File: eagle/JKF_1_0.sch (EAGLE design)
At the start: 14 parts, among them IC1 74HC107N, X1 In A, X2 In B, X3 Ctrl, X4 Out A, X5 Out B

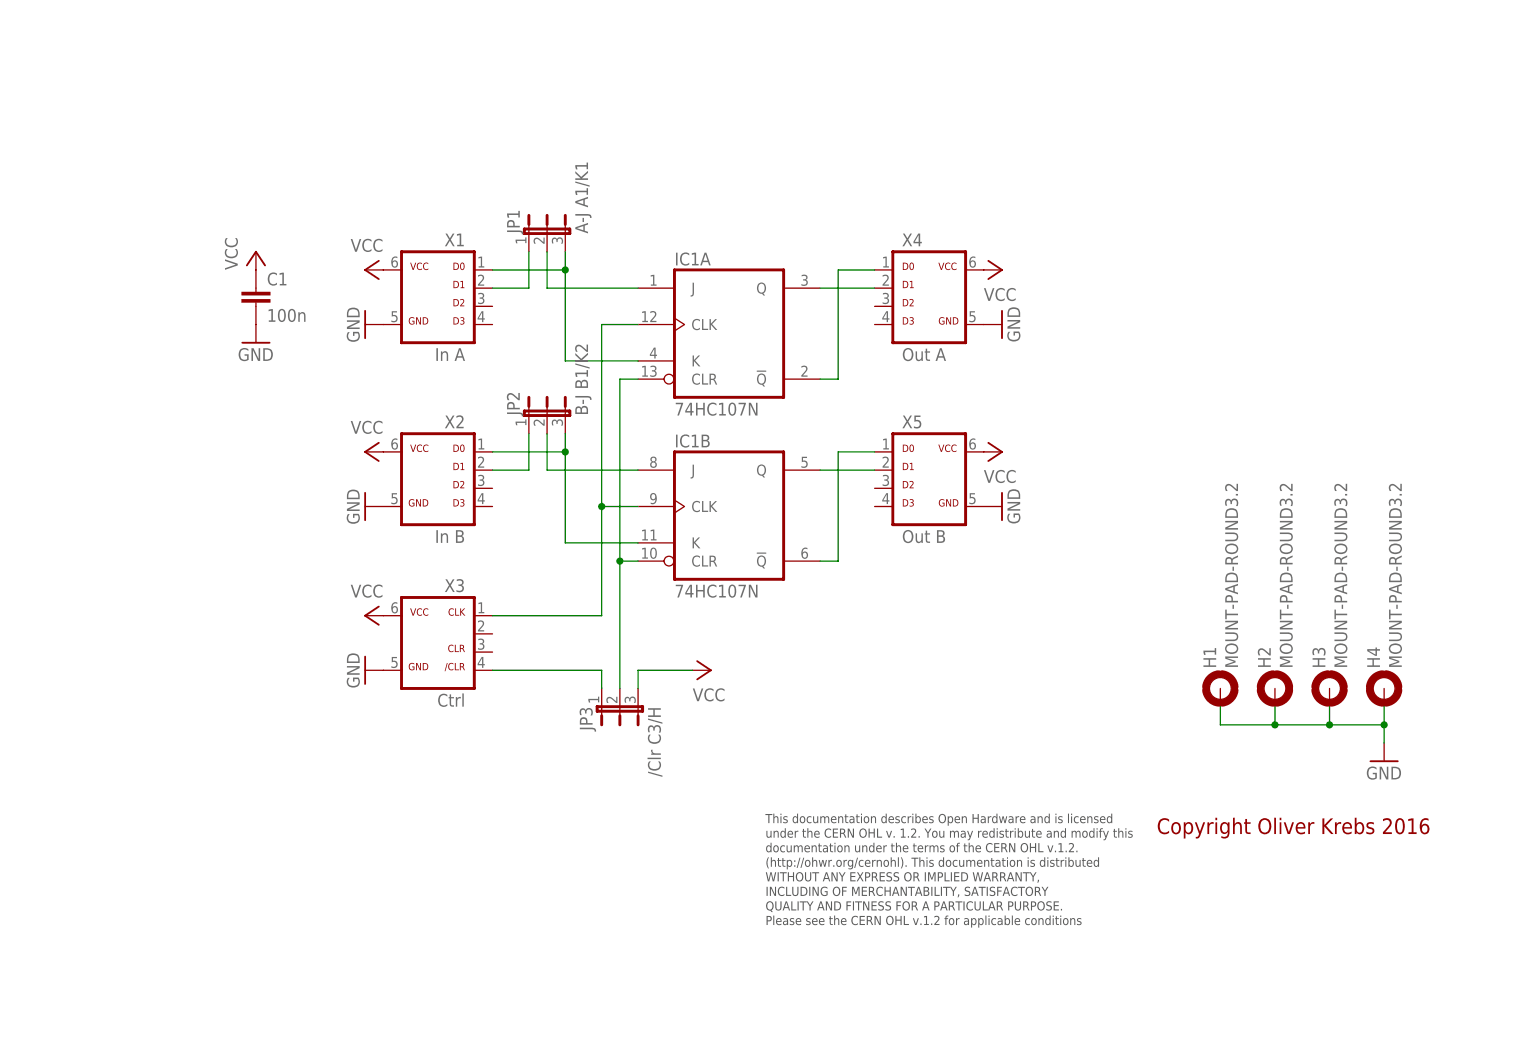
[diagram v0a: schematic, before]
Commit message: Add new tetra-Board and arduino files
Add AMP_1_0, AVC_1_0, D18_1_1, IOP_1_2, MIC_1_0, PIN_1_1, POT_1_0, PWA_1_0, PWR_1_0, RGF 2.0, SOC_2_0, VLT_1_0
Add mex_nano_shield_keyboard, mex_nano_shied_numbers

New arduino projects
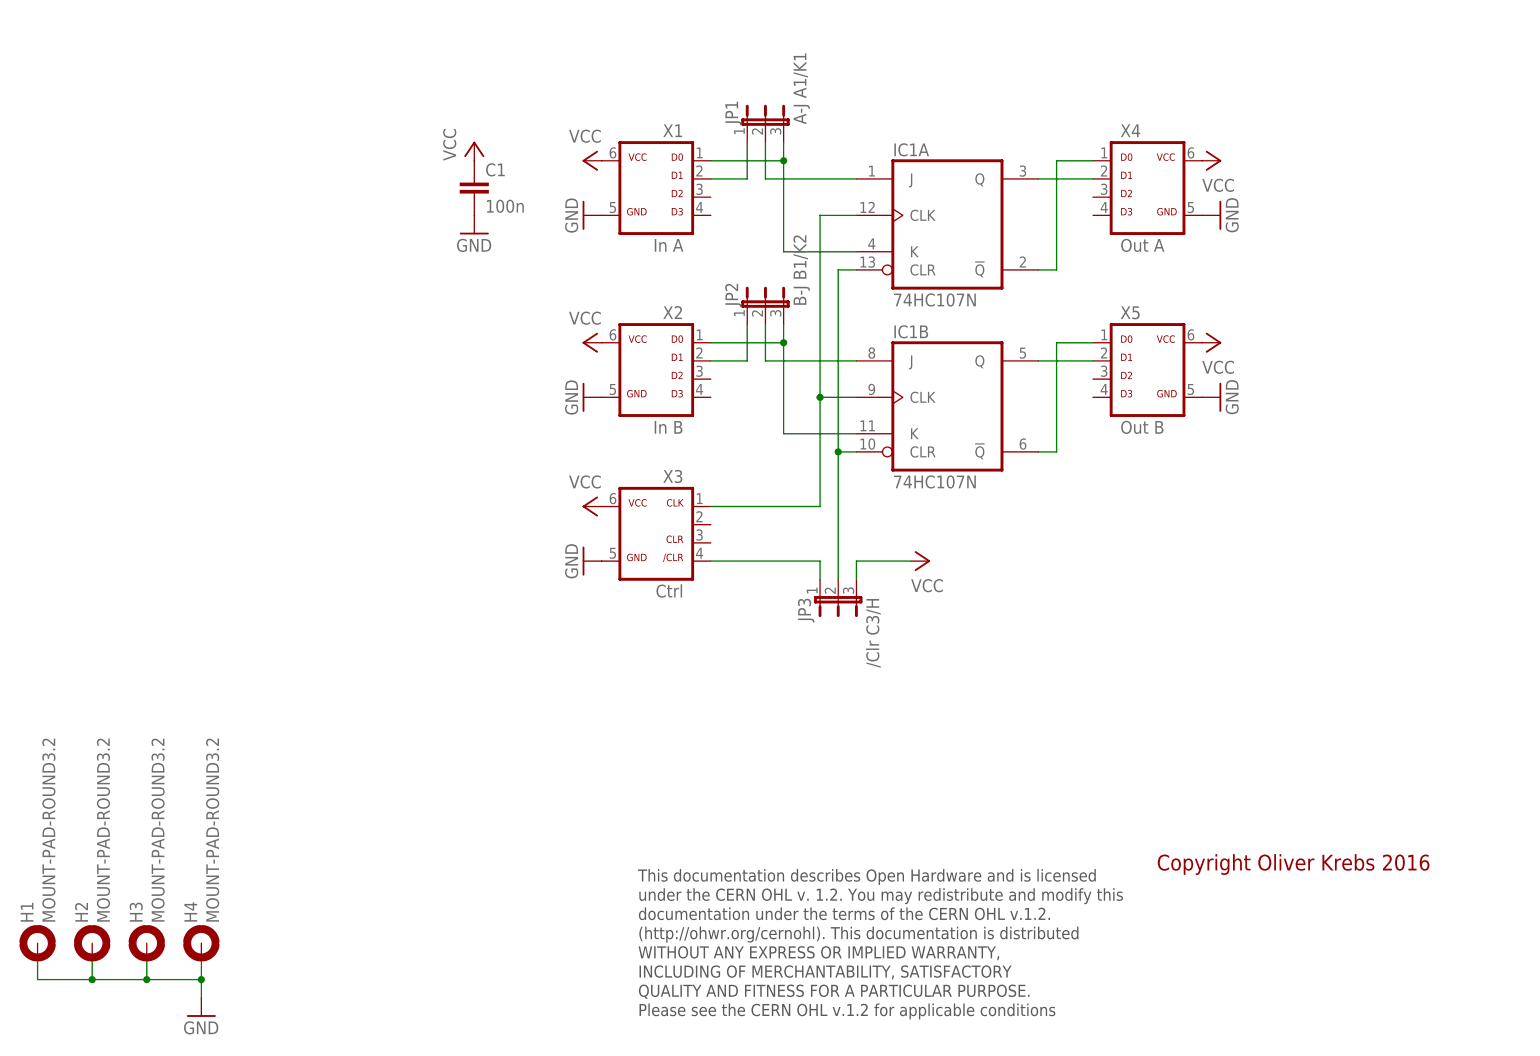
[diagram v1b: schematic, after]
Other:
- moved on the sheet: C1, H1, H2, H3, H4, IC1A, IC1B, JP1, JP2, JP3, X1, X2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
